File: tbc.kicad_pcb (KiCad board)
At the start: 4 copper layers, 180 x 67 mm, 118 parts, among them J1 5749181-1, J2 PJRAN1X1U01X, J3 PJRAN1X1U01X, J4 5749181-1, J5 PJRAN1X1U01X, J6 PJRAN3X1U03X, J7 4840.2201, J8 20021111-00010T4LF, Q1 BSS308PE, SW1 1825910-6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

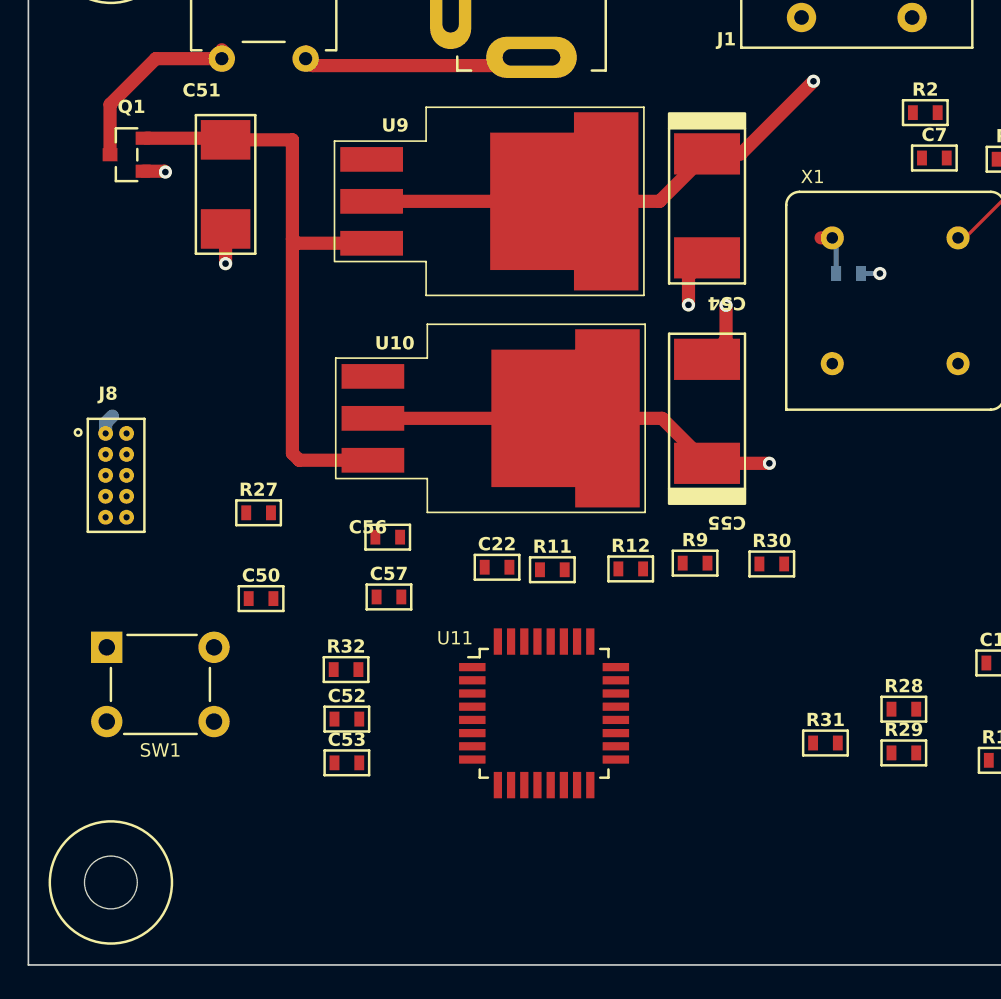
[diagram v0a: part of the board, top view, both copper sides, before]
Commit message: added connector and diode footprint, more layout
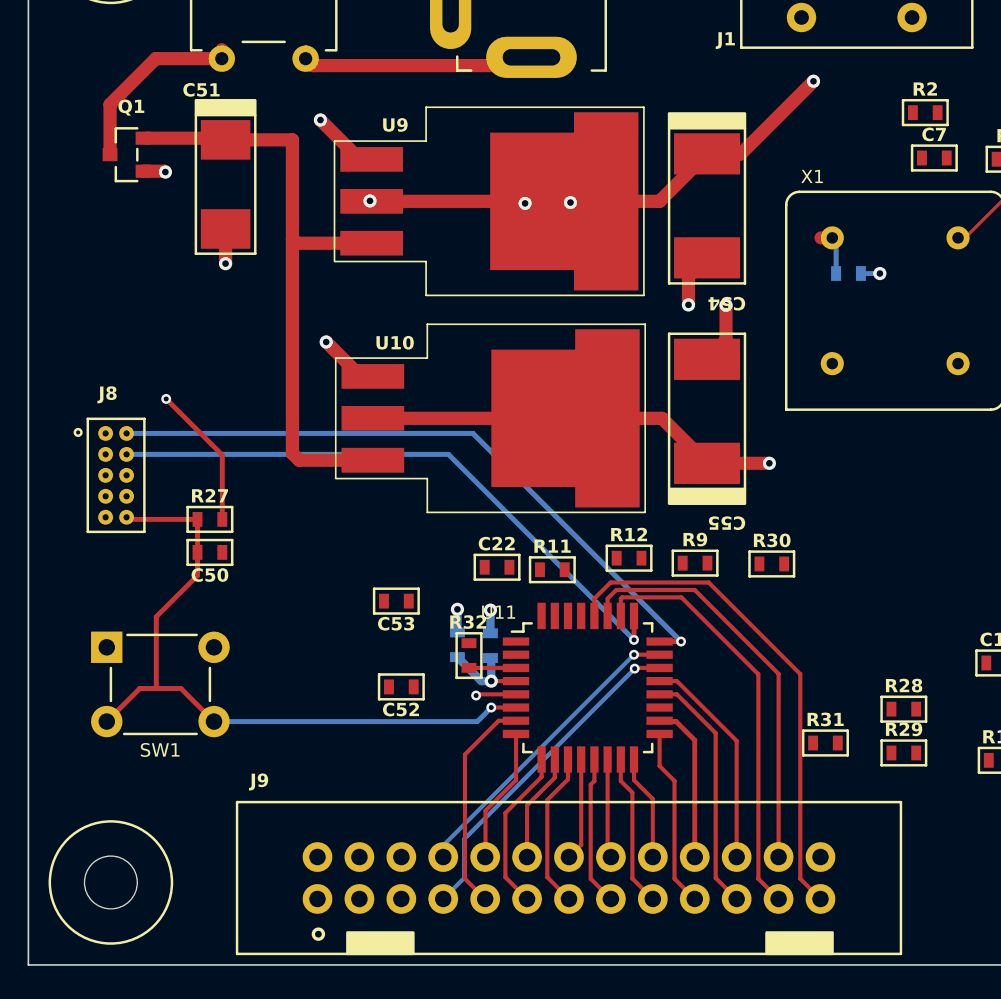
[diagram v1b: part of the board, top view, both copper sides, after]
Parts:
- added J9: 75869-105LF, tbc:75869-105LF, F.Cu at (112.8, 126.7)
- C56, C57: moved to B.Cu
- moved C53 10.2 mm to (102.3, 110.0), turned to 180 degrees
- moved C56 7.77 mm to (106.0, 112.6), turned to 90 degrees
- moved R32 7.50 mm to (106.7, 113.2), turned to 90 degrees
- moved C57 6.82 mm to (108.0, 112.7), turned to 90 degrees
- moved C50 4.18 mm to (91.0, 107.0), turned to 180 degrees
- moved C52 3.83 mm to (102.6, 115.2), turned to 180 degrees
- moved U11 3.07 mm to (113.9, 115.2)
- moved R27 2.98 mm to (91.0, 105.0)
- moved R12 0.66 mm to (116.4, 107.3)
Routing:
- net +3V3: track 268.5 -> 391.3 mm, vias 18 -> 23
- net +5V: track 226.0 -> 281.2 mm
- net Net-(U11-PF2-NRST): track 0.00 -> 42.4 mm, vias 0 -> 1
- net Net-(U11-PA13): track 0.00 -> 40.1 mm, vias 0 -> 1
- net Net-(U11-PA14-BOOT0): track 0.00 -> 36.9 mm, vias 0 -> 1
- net /Microcontroller, Power/EXP_9: track 0.00 -> 30.4 mm
- net /Microcontroller, Power/EXP_7: track 0.00 -> 25.5 mm
- net /Microcontroller, Power/EXP_8: track 0.00 -> 24.8 mm
- net /Microcontroller, Power/SCL2: track 0.00 -> 20.3 mm, vias 0 -> 1
- net /Microcontroller, Power/SDA2: track 0.00 -> 18.6 mm, vias 0 -> 1
- net /Microcontroller, Power/EXP_5: track 0.00 -> 14.9 mm
- net /Microcontroller, Power/D_READY: track 0.00 -> 13.4 mm
- net /Microcontroller, Power/EXP_6: track 0.00 -> 13.2 mm
- net GND: track 140.1 -> 153.1 mm, vias 71 -> 76
- net /Microcontroller, Power/RENC_SW: track 0.00 -> 10.9 mm
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
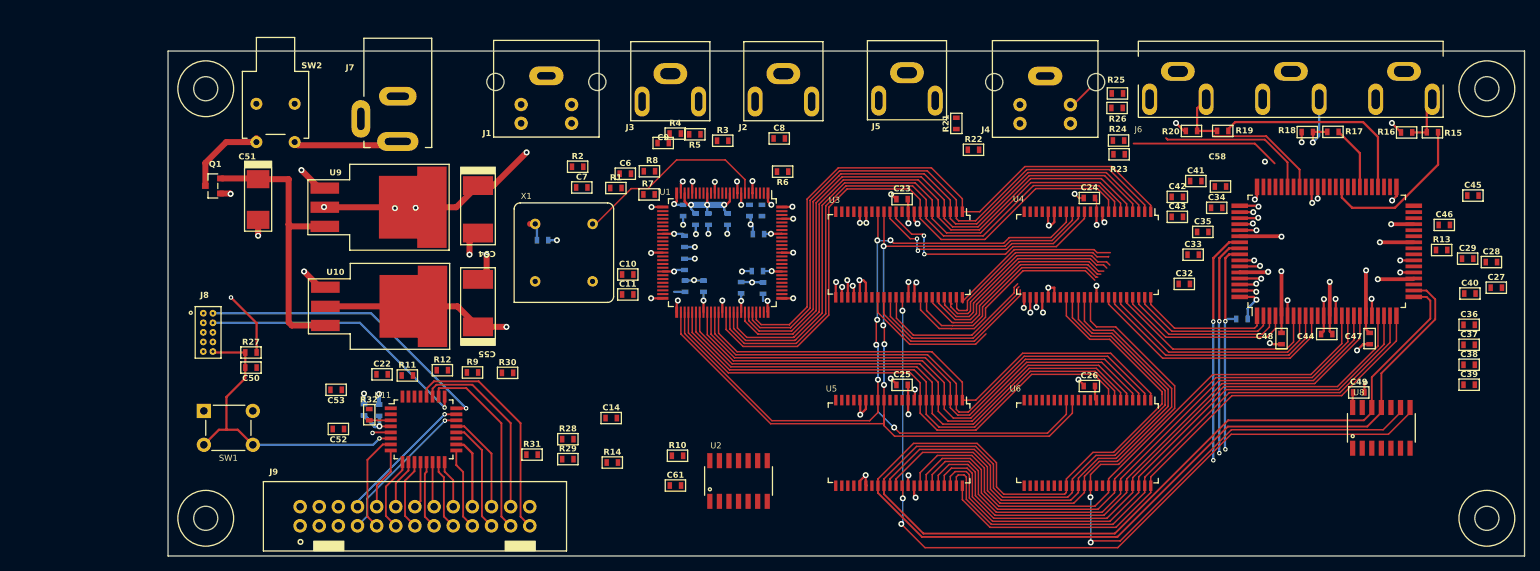
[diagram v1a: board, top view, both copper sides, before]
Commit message: added footprints for crystals and updated layout
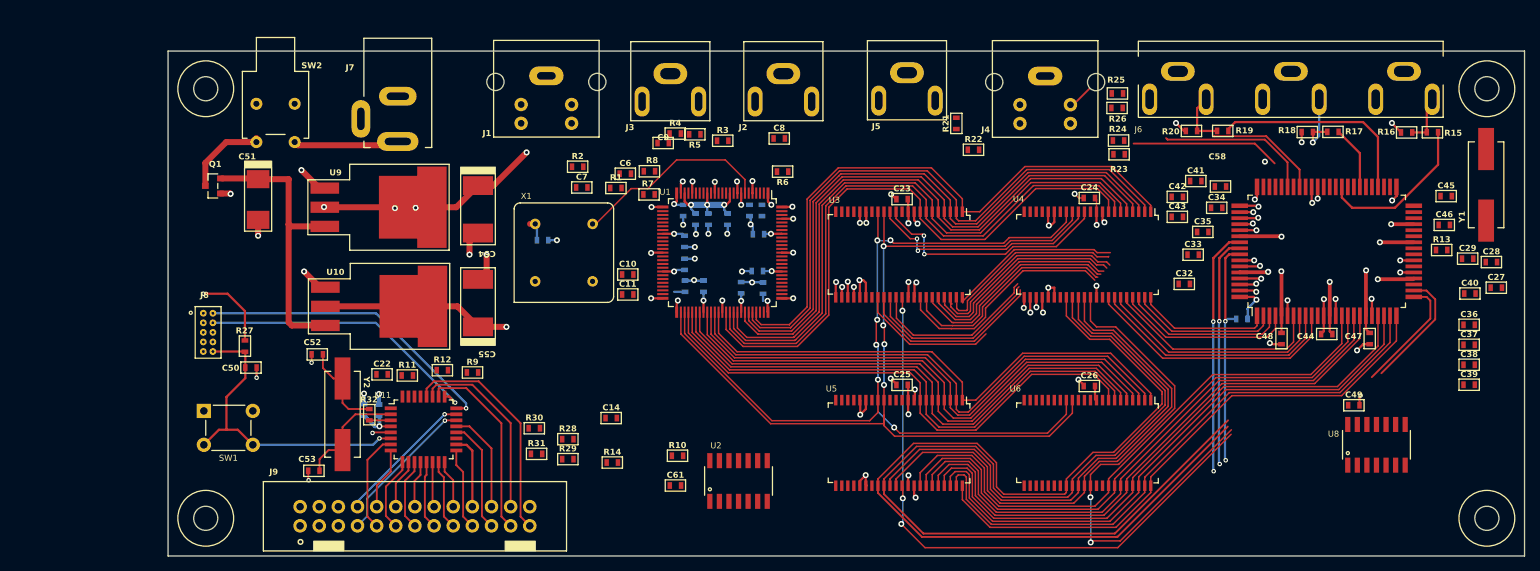
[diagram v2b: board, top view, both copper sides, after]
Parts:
- added Y1: ABLS-27.000MHZ-B2F-T, tbc:ABLS, F.Cu at (254.9, 82.8)
- added Y2: ABLS2-8.000MHZ-D4Y-T, tbc:ABLS2, F.Cu at (103.2, 113.2)
- moved C53 11.1 mm to (99.3, 120.7)
- moved C52 10.3 mm to (99.8, 105.2)
- moved R30 8.16 mm to (128.6, 115.0)
- moved C45 3.55 mm to (249.6, 84.2)
- moved U8 2.34 mm to (240.3, 117.2)
- moved C49 1.82 mm to (237.3, 112.0)
- moved R27 1.17 mm to (90.2, 104.2), turned to 90 degrees
- moved R31 0.61 mm to (128.9, 118.5)
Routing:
- net /Frame Memories and Freeze/RCV2: track 189.2 -> 162.8 mm
- net /Frame Memories and Freeze/Q2: track 108.7 -> 83.1 mm
- net /Frame Memories and Freeze/RCV1: track 191.9 -> 167.7 mm
- net /Frame Memories and Freeze/Q1: track 93.6 -> 69.6 mm
- net Net-(U11-PC14-OSC32_IN): track 0.00 -> 15.3 mm
- net Net-(C52-Pad1): track 0.00 -> 12.1 mm
- net GND: track 153.1 -> 163.1 mm, vias 76 -> 79
- net +3V3: track 391.3 -> 394.6 mm
- net +5V: track 281.2 -> 279.2 mm
- net /Microcontroller, Power/SCL: track 31.2 -> 32.7 mm
- net /Microcontroller, Power/VENC_RST: track 29.1 -> 30.6 mm
- net Net-(U11-PA14-BOOT0): track 36.9 -> 38.3 mm
- net /Microcontroller, Power/SDA: track 29.2 -> 30.6 mm

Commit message: 3V3A component footprints + layout work
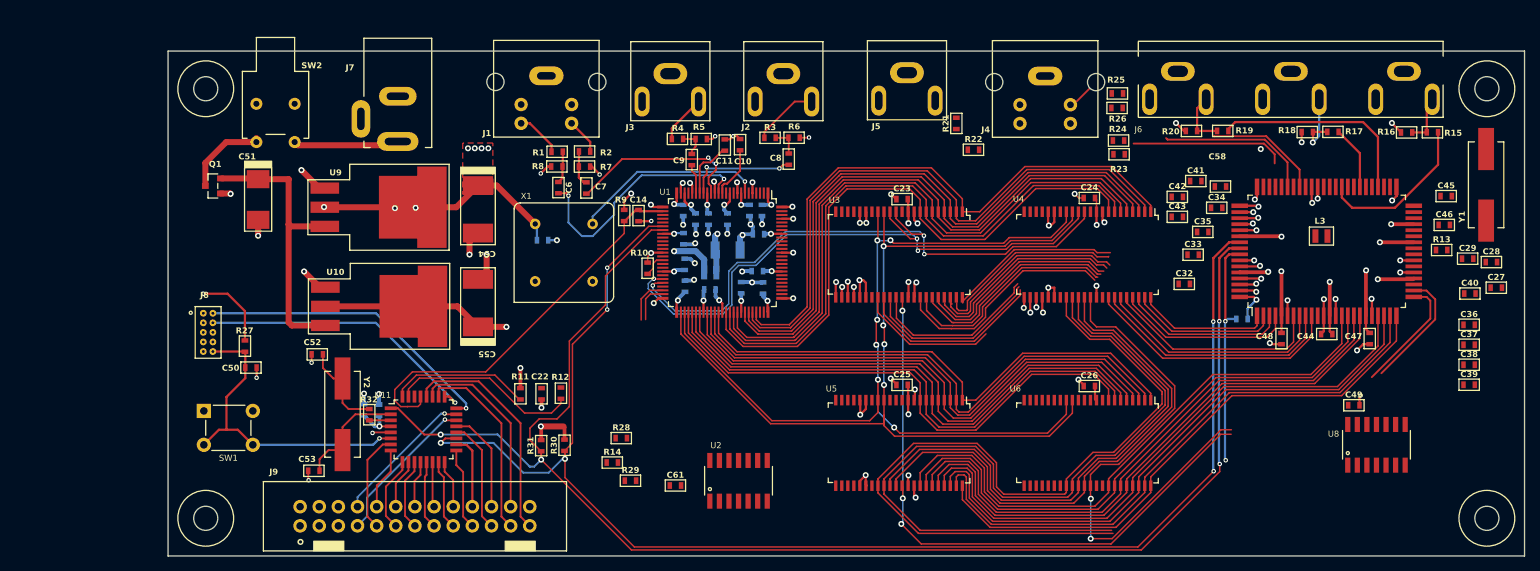
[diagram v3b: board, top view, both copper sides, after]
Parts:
- added C1: 22u|25V, tbc:GRM32, B.Cu at (154.2, 91.4)
- added L1: 10uH, tbc:DFE201610E, B.Cu at (151.9, 94.4)
- added L3: 10uH, tbc:DFE201610E, F.Cu at (233.1, 89.5)
- moved R9 29.0 mm to (140.5, 86.8), turned to -90 degrees
- moved C14 27.1 mm to (142.4, 86.8), turned to 90 degrees
- moved R10 25.2 mm to (143.6, 93.8), turned to 90 degrees
- moved C11 23.6 mm to (153.9, 77.5), turned to -90 degrees
- moved C10 22.8 mm to (155.9, 77.4), turned to -90 degrees
- moved C22 21.3 mm to (129.6, 110.5), turned to 90 degrees
- moved R12 16.0 mm to (132.1, 110.4), turned to 90 degrees
- moved R11 15.2 mm to (126.8, 110.5), turned to 90 degrees
- moved R8 12.3 mm to (131.6, 80.3), turned to 0 degrees
- moved R7 9.33 mm to (135.3, 80.3)
- moved R1 9.16 mm to (131.6, 78.4)
- moved C6 9.06 mm to (131.8, 83.1), turned to -90 degrees
- moved R29 8.79 mm to (141.4, 122.0)
- moved R28 7.09 mm to (140.1, 116.4)
- moved R3 6.29 mm to (159.9, 76.5)
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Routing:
- net /Microcontroller, Power/SDA: track 30.6 -> 195.3 mm, vias 2 -> 4
- net /Microcontroller, Power/SCL: track 32.7 -> 188.0 mm, vias 2 -> 6
- net /Microcontroller, Power/VDEC_RST: track 0.00 -> 52.8 mm
- net +3V3: track 394.6 -> 343.5 mm, vias 23 -> 29
- net /Frame Memories and Freeze/ICLK: track 31.5 -> 78.5 mm, vias 2 -> 3
- net /Frame Memories and Freeze/IDQ: track 32.3 -> 78.7 mm, vias 2 -> 3
- net Net-(U1-AI22): track 0.00 -> 33.1 mm, vias 0 -> 2
- net /Frame Memories and Freeze/MEM_MODE: track 0.00 -> 24.9 mm
- net Net-(U1-AI21): track 0.00 -> 23.9 mm, vias 0 -> 2
- net /Frame Memories and Freeze/RCV1: track 167.7 -> 145.8 mm
- net /Frame Memories and Freeze/RCV2: track 162.8 -> 141.3 mm
- net /Frame Memories and Freeze/MEM_CLR: track 0.00 -> 18.8 mm
- net GND: track 163.1 -> 181.0 mm, vias 79 -> 88
- net Net-(U1-AI12): track 0.00 -> 14.8 mm, vias 0 -> 2
- net +3V3A: track 14.1 -> 23.2 mm, vias 3 -> 4
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- added copper zone on F.Cu, net +3V3
- added copper zone on In2.Cu, net +3V3

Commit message: layout LHS
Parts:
- added C31: 22u|25V, tbc:GRM32, F.Cu at (233.7, 92.7)
- moved R14 9.79 mm to (129.4, 117.2), turned to -90 degrees
- moved C61 8.69 mm to (152.7, 115.8), turned to 180 degrees
- moved R29 4.85 mm to (141.8, 117.2), turned to 90 degrees
- moved R31 3.05 mm to (132.6, 117.3)
- moved R30 3.05 mm to (135.7, 117.2)
- moved R28 1.52 mm to (138.8, 117.1), turned to 90 degrees
- moved C8 0.48 mm to (162.5, 79.8)
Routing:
- net /Frame Memories and Freeze/MEM_CLR: track 18.8 -> 209.3 mm, vias 0 -> 2
- net /Microcontroller, Power/VENC_RST: track 30.6 -> 157.2 mm, vias 2 -> 4
- net +5V: track 281.9 -> 346.7 mm, vias 19 -> 25
- net /Frame Memories and Freeze/FREEZE: track 0.00 -> 59.6 mm, vias 0 -> 1
- net /Frame Memories and Freeze/MEM_MODE: track 24.9 -> 70.8 mm, vias 0 -> 3
- net /Frame Memories and Freeze/IGP0: track 6.15 -> 38.2 mm
- net /Microcontroller, Power/SDA2: track 19.0 -> 48.8 mm, vias 1 -> 2
- net /Microcontroller, Power/SCL2: track 20.5 -> 47.8 mm, vias 1 -> 2
- net /Frame Memories and Freeze/IGP1: track 5.29 -> 29.6 mm
- net /Frame Memories and Freeze/IGPV: track 120.7 -> 105.0 mm, vias 4 -> 2
- net /Frame Memories and Freeze/RCV2: track 141.3 -> 156.8 mm
- net +3V3: track 343.5 -> 357.6 mm, vias 29 -> 33
- net Net-(U2-1Y): track 0.00 -> 12.1 mm
- net /Frame Memories and Freeze/CREF: track 93.3 -> 104.1 mm
- net /Frame Memories and Freeze/LLC: track 94.6 -> 104.4 mm
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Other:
- board text added: "Time Base Corrector and Scaler https://github.com/philmcm/tbc Version ${VERSION}"

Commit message: extra bypass cap for memories + more layout
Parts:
- added C62: 100n, tbc:C0603, B.Cu at (179.0, 94.3)
- added C63: 100n, tbc:C0603, B.Cu at (202.5, 94.8)
- added C64: 100n, tbc:C0603, B.Cu at (179.1, 120.0)
- added C65: 100n, tbc:C0603, B.Cu at (204.1, 119.8)
- C23, C24, C25, C26: moved to B.Cu
- moved C25 5.48 mm to (179.0, 114.5), turned to 180 degrees
- moved C26 5.39 mm to (204.1, 114.5), turned to 180 degrees
- moved C24 4.98 mm to (202.5, 89.5)
- moved C23 4.79 mm to (179.1, 89.2), turned to 180 degrees
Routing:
- net Net-(U2-2Y): track 0.00 -> 96.8 mm, vias 0 -> 3
- net /Frame Memories and Freeze/MEM_MODE: track 70.8 -> 158.0 mm, vias 3 -> 4
- net /Frame Memories and Freeze/MEM_CLR: track 209.3 -> 277.6 mm, vias 2 -> 7
- net /Frame Memories and Freeze/ICLK: track 78.8 -> 144.2 mm
- net /Frame Memories and Freeze/IDQ: track 79.0 -> 141.9 mm
- net Net-(U2-3Y): track 2.58 -> 58.8 mm, vias 1 -> 3
- net GND: track 189.2 -> 233.8 mm, vias 90 -> 110
- net /Frame Memories and Freeze/IGPV: track 105.0 -> 126.0 mm, vias 2 -> 4
- net /Microcontroller, Power/VDEC_RST: track 52.8 -> 60.5 mm
- net +5V: track 346.7 -> 354.4 mm
- net /Frame Memories and Freeze/IGP1: track 29.6 -> 36.4 mm
- net /Frame Memories and Freeze/IGPH: track 119.0 -> 123.0 mm, vias 3 -> 2
- net /Frame Memories and Freeze/DP1: track 51.9 -> 54.6 mm
- net /Frame Memories and Freeze/DP7: track 66.8 -> 69.3 mm
- net /Frame Memories and Freeze/HPD5: track 80.4 -> 82.9 mm
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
